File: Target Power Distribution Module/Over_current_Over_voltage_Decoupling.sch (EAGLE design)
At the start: 5 parts

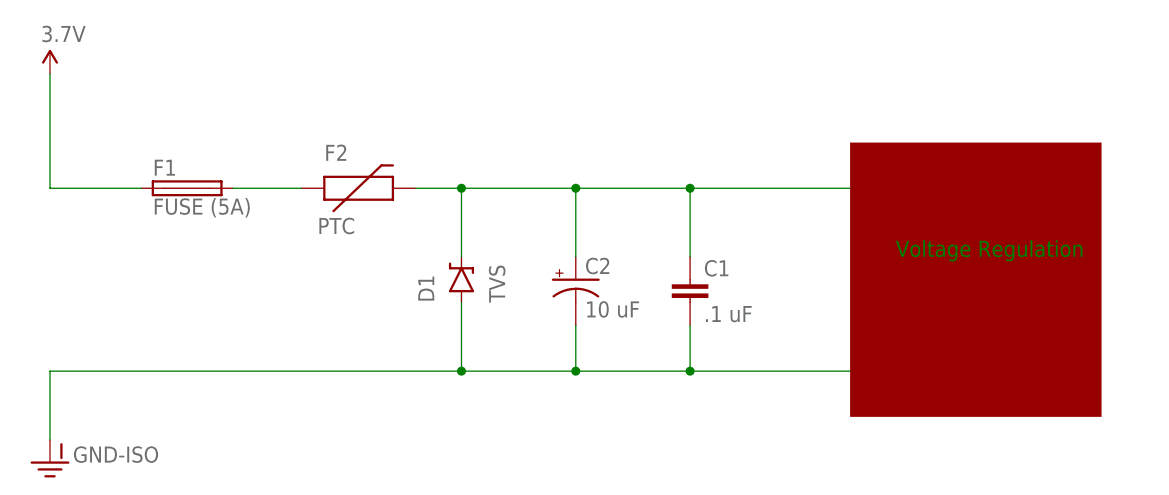
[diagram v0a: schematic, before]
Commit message: Added battery and battery connector
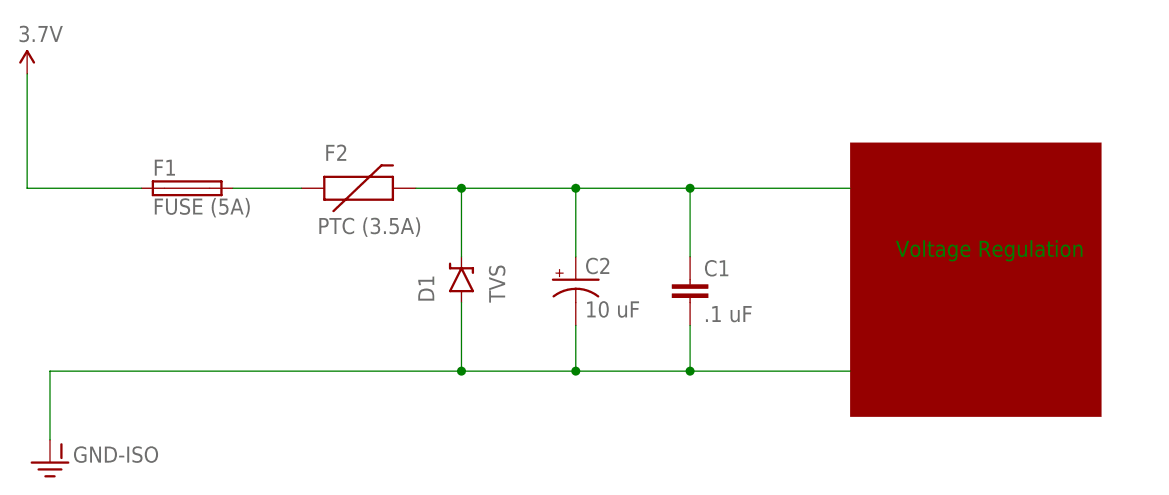
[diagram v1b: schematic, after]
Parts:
- F2: value PTC -> PTC (3.5A)
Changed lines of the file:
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@@
 <grid distance="0.1" unitdist="inch" unit="inch" style="lines" multiple="1" display="no" altdistance="0.01" altunitdist="inch" altunit="inch"/>
 <layers>
-<layer number="1" name="Top" color="4" fill="1" visible="no" active="no"/>
-<layer number="16" name="Bottom" color="1" fill="1" visible="no" active="no"/>
-<layer number="17" name="Pads" color="2" fill="1" visible="no" active="no"/>
-<layer number="18" name="Vias" color="2" fill="1" visible="no" active="no"/>
-<layer number="19" name="Unrouted" color="6" fill="1" visible="no" active="no"/>
-<layer number="20" name="Dimension" color="15" fill="1" visible="no" active="no"/>
-<layer number="21" name="tPlace" color="16" fill="1" visible="no" active="no"/>
-<layer number="22" name="bPlace" color="7" fill="1" visible="no" active="no"/>
-<layer number="23" name="tOrigins" color="15" fill="1" visible="no" active="no"/>
-<layer number="24" name="bOrigins" color="15" fill="1" visible="no" active="no"/>
-<layer number="25" name="tNames" color="7" fill="1" visible="no" active="no"/>
-<layer number="26" name="bNames" color="7" fill="1" visible="no" active="no"/>
-<layer number="27" name="tValues" color="7" fill="1" visible="no" active="no"/>
-<layer number="28" name="bValues" color="7" fill="1" visible="no" active="no"/>
+<layer number="1" name="Top" color="4" fill="1" visible="yes" active="no"/>
+<layer number="16" name="Bottom" color="1" fill="1" visible="yes" active="no"/>
+<layer number="17" name="Pads" color="2" fill="1" visible="yes" active="no"/>
+<layer number="18" name="Vias" color="2" fill="1" visible="yes" active="no"/>
+<layer number="19" name="Unrouted" color="6" fill="1" visible="yes" active="no"/>
+<layer number="20" name="Dimension" color="15" fill="1" visible="yes" active="no"/>
+<layer number="21" name="tPlace" color="16" fill="1" visible="yes" active="no"/>
+<layer number="22" name="bPlace" color="7" fill="1" visible="yes" active="no"/>
+<layer number="23" name="tOrigins" color="15" fill="1" visible="yes" active="no"/>
+<layer number="24" name="bOrigins" color="15" fill="1" visible="yes" active="no"/>
+<layer number="25" name="tNames" color="7" fill="1" visible="yes" active="no"/>
+<layer number="26" name="bNames" color="7" fill="1" visible="yes" active="no"/>
+<layer number="27" name="tValues" color="7" fill="1" visible="yes" active="no"/>
+<layer number="28" name="bValues" color="7" fill="1" visible="yes" active="no"/>
 <layer number="29" name="tStop" color="7" fill="3" visible="no" active="no"/>
 <layer number="30" name="bStop" color="7" fill="6" visible="no" active="no"/>
@@
 <layer number="35" name="tGlue" color="7" fill="4" visible="no" active="no"/>
 <layer number="36" name="bGlue" color="7" fill="5" visible="no" active="no"/>
-<layer number="37" name="tTest" color="7" fill="1" visible="no" active="no"/>
-<layer number="38" name="bTest" color="7" fill="1" visible="no" active="no"/>
+<layer number="37" name="tTest" color="7" fill="1" visible="yes" active="no"/>
+<layer number="38" name="bTest" color="7" fill="1" visible="yes" active="no"/>
 <layer number="39" name="tKeepout" color="4" fill="11" visible="no" active="no"/>
 <layer number="40" name="bKeepout" color="1" fill="11" visible="no" active="no"/>
@@
 <layer number="44" name="Drills" color="7" fill="1" visible="no" active="no"/>
 <layer number="45" name="Holes" color="7" fill="1" visible="no" active="no"/>
-<layer number="46" name="Milling" color="3" fill="1" visible="no" active="no"/>
-<layer number="47" name="Measures" color="7" fill="1" visible="no" active="no"/>
-<layer number="48" name="Document" color="7" fill="1" visible="no" active="no"/>
-<layer number="49" name="Reference" color="7" fill="1" visible="no" active="no"/>
-<layer number="50" name="dxf" color="7" fill="1" visible="no" active="no"/>
-<layer number="51" name="tDocu" color="14" fill="1" visible="no" active="no"/>
-<layer number="52" name="bDocu" color="7" fill="1" visible="no" active="no"/>
-<layer number="53" name="tGND_GNDA" color="7" fill="9" visible="no" active="no"/>
-<layer number="54" name="bGND_GNDA" color="1" fill="9" visible="no" active="no"/>
-<layer number="56" name="wert" color="7" fill="1" visible="no" active="no"/>
-<layer number="57" name="tCAD" color="7" fill="1" visible="no" active="no"/>
-<layer number="59" name="tCarbon" color="7" fill="1" visible="no" active="no"/>
-<layer number="60" name="bCarbon" color="7" fill="1" visible="no" active="no"/>
+<layer number="46" name="Milling" color="3" fill="1" visible="yes" active="no"/>
+<layer number="47" name="Measures" color="7" fill="1" visible="yes" active="no"/>
+<layer number="48" name="Document" color="7" fill="1" visible="yes" active="no"/>
+<layer number="49" name="Reference" color="7" fill="1" visible="yes" active="no"/>
+<layer number="50" name="dxf" color="7" fill="1" visible="yes" active="no"/>
+<layer number="51" name="tDocu" color="14" fill="1" visible="yes" active="no"/>
+<layer number="52" name="bDocu" color="7" fill="1" visible="yes" active="no"/>
+<layer number="53" name="tGND_GNDA" color="7" fill="9" visible="yes" active="no"/>
+<layer number="54" name="bGND_GNDA" color="1" fill="9" visible="yes" active="no"/>
+<layer number="56" name="wert" color="7" fill="1" visible="yes" active="no"/>
+<layer number="57" name="tCAD" color="7" fill="1" visible="yes" active="no"/>
+<layer number="59" name="tCarbon" color="7" fill="1" visible="yes" active="no"/>
+<layer number="60" name="bCarbon" color="7" fill="1" visible="yes" active="no"/>
 <layer number="90" name="Modules" color="5" fill="1" visible="yes" active="yes"/>
 <layer number="91" name="Nets" color="2" fill="1" visible="yes" active="yes"/>
@@
 <part name="D1" library="SparkFun-DiscreteSemi" deviceset="DIODE-ZENER" device="PTH" value="TVS"/>
 <part name="F1" library="fuse" deviceset="FUSE" device="1821" value="FUSE (5A)"/>
-<part name="F2" library="SparkFun-PowerIC" deviceset="PTC" device="PTH" value="PTC"/>
+<part name="F2" library="SparkFun-PowerIC" deviceset="PTC" device="PTH" value="PTC (3.5A)"/>
 <part name="C1" library="SparkFun-Capacitors" deviceset="CAP" device="1206" value=".1 uF"/>
 <part name="C2" library="SparkFun-Passives" deviceset="CAP_POL" device="PTH2" value="10 uF"/>
@@
 <instance part="C2" gate="G$1" x="40.64" y="53.34"/>
 <instance part="GND-ISO1" gate="G$1" x="-17.78" y="33.02"/>
-<instance part="SUPPLY1" gate="G$1" x="-17.78" y="76.2"/>
+<instance part="SUPPLY1" gate="G$1" x="-20.32" y="76.2"/>
 </instances>
 <busses>
@@
 <segment>
 <pinref part="F1" gate="G$1" pin="1"/>
-<wire x1="-7.62" y1="63.5" x2="-17.78" y2="63.5" width="0.1524" layer="91"/>
-<wire x1="-17.78" y1="63.5" x2="-17.78" y2="76.2" width="0.1524" layer="91"/>
+<wire x1="-7.62" y1="63.5" x2="-20.32" y2="63.5" width="0.1524" layer="91"/>
+<wire x1="-20.32" y1="63.5" x2="-20.32" y2="76.2" width="0.1524" layer="91"/>
 <pinref part="SUPPLY1" gate="G$1" pin="VCC"/>
 </segment>

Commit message: Test text
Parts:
- F1: value FUSE (5A) -> FUSE (2A)
- F2: value PTC (3.5A) -> PTC (1.5A)
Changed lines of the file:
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@@
 <grid distance="0.1" unitdist="inch" unit="inch" style="lines" multiple="1" display="no" altdistance="0.01" altunitdist="inch" altunit="inch"/>
 <layers>
-<layer number="1" name="Top" color="4" fill="1" visible="yes" active="no"/>
-<layer number="16" name="Bottom" color="1" fill="1" visible="yes" active="no"/>
-<layer number="17" name="Pads" color="2" fill="1" visible="yes" active="no"/>
-<layer number="18" name="Vias" color="2" fill="1" visible="yes" active="no"/>
-<layer number="19" name="Unrouted" color="6" fill="1" visible="yes" active="no"/>
-<layer number="20" name="Dimension" color="15" fill="1" visible="yes" active="no"/>
-<layer number="21" name="tPlace" color="16" fill="1" visible="yes" active="no"/>
-<layer number="22" name="bPlace" color="7" fill="1" visible="yes" active="no"/>
-<layer number="23" name="tOrigins" color="15" fill="1" visible="yes" active="no"/>
-<layer number="24" name="bOrigins" color="15" fill="1" visible="yes" active="no"/>
-<layer number="25" name="tNames" color="7" fill="1" visible="yes" active="no"/>
-<layer number="26" name="bNames" color="7" fill="1" visible="yes" active="no"/>
-<layer number="27" name="tValues" color="7" fill="1" visible="yes" active="no"/>
-<layer number="28" name="bValues" color="7" fill="1" visible="yes" active="no"/>
+<layer number="1" name="Top" color="4" fill="1" visible="no" active="no"/>
+<layer number="16" name="Bottom" color="1" fill="1" visible="no" active="no"/>
+<layer number="17" name="Pads" color="2" fill="1" visible="no" active="no"/>
+<layer number="18" name="Vias" color="2" fill="1" visible="no" active="no"/>
+<layer number="19" name="Unrouted" color="6" fill="1" visible="no" active="no"/>
+<layer number="20" name="Dimension" color="15" fill="1" visible="no" active="no"/>
+<layer number="21" name="tPlace" color="16" fill="1" visible="no" active="no"/>
+<layer number="22" name="bPlace" color="7" fill="1" visible="no" active="no"/>
+<layer number="23" name="tOrigins" color="15" fill="1" visible="no" active="no"/>
+<layer number="24" name="bOrigins" color="15" fill="1" visible="no" active="no"/>
+<layer number="25" name="tNames" color="7" fill="1" visible="no" active="no"/>
+<layer number="26" name="bNames" color="7" fill="1" visible="no" active="no"/>
+<layer number="27" name="tValues" color="7" fill="1" visible="no" active="no"/>
+<layer number="28" name="bValues" color="7" fill="1" visible="no" active="no"/>
 <layer number="29" name="tStop" color="7" fill="3" visible="no" active="no"/>
 <layer number="30" name="bStop" color="7" fill="6" visible="no" active="no"/>
@@
 <layer number="35" name="tGlue" color="7" fill="4" visible="no" active="no"/>
 <layer number="36" name="bGlue" color="7" fill="5" visible="no" active="no"/>
-<layer number="37" name="tTest" color="7" fill="1" visible="yes" active="no"/>
-<layer number="38" name="bTest" color="7" fill="1" visible="yes" active="no"/>
+<layer number="37" name="tTest" color="7" fill="1" visible="no" active="no"/>
+<layer number="38" name="bTest" color="7" fill="1" visible="no" active="no"/>
 <layer number="39" name="tKeepout" color="4" fill="11" visible="no" active="no"/>
 <layer number="40" name="bKeepout" color="1" fill="11" visible="no" active="no"/>
@@
 <layer number="44" name="Drills" color="7" fill="1" visible="no" active="no"/>
 <layer number="45" name="Holes" color="7" fill="1" visible="no" active="no"/>
-<layer number="46" name="Milling" color="3" fill="1" visible="yes" active="no"/>
-<layer number="47" name="Measures" color="7" fill="1" visible="yes" active="no"/>
-<layer number="48" name="Document" color="7" fill="1" visible="yes" active="no"/>
-<layer number="49" name="Reference" color="7" fill="1" visible="yes" active="no"/>
-<layer number="50" name="dxf" color="7" fill="1" visible="yes" active="no"/>
-<layer number="51" name="tDocu" color="14" fill="1" visible="yes" active="no"/>
-<layer number="52" name="bDocu" color="7" fill="1" visible="yes" active="no"/>
-<layer number="53" name="tGND_GNDA" color="7" fill="9" visible="yes" active="no"/>
-<layer number="54" name="bGND_GNDA" color="1" fill="9" visible="yes" active="no"/>
-<layer number="56" name="wert" color="7" fill="1" visible="yes" active="no"/>
-<layer number="57" name="tCAD" color="7" fill="1" visible="yes" active="no"/>
-<layer number="59" name="tCarbon" color="7" fill="1" visible="yes" active="no"/>
-<layer number="60" name="bCarbon" color="7" fill="1" visible="yes" active="no"/>
+<layer number="46" name="Milling" color="3" fill="1" visible="no" active="no"/>
+<layer number="47" name="Measures" color="7" fill="1" visible="no" active="no"/>
+<layer number="48" name="Document" color="7" fill="1" visible="no" active="no"/>
+<layer number="49" name="Reference" color="7" fill="1" visible="no" active="no"/>
+<layer number="50" name="dxf" color="7" fill="1" visible="no" active="no"/>
+<layer number="51" name="tDocu" color="14" fill="1" visible="no" active="no"/>
+<layer number="52" name="bDocu" color="7" fill="1" visible="no" active="no"/>
+<layer number="53" name="tGND_GNDA" color="7" fill="9" visible="no" active="no"/>
+<layer number="54" name="bGND_GNDA" color="1" fill="9" visible="no" active="no"/>
+<layer number="56" name="wert" color="7" fill="1" visible="no" active="no"/>
+<layer number="57" name="tCAD" color="7" fill="1" visible="no" active="no"/>
+<layer number="59" name="tCarbon" color="7" fill="1" visible="no" active="no"/>
+<layer number="60" name="bCarbon" color="7" fill="1" visible="no" active="no"/>
 <layer number="90" name="Modules" color="5" fill="1" visible="yes" active="yes"/>
 <layer number="91" name="Nets" color="2" fill="1" visible="yes" active="yes"/>
@@
 <parts>
 <part name="D1" library="SparkFun-DiscreteSemi" deviceset="DIODE-ZENER" device="PTH" value="TVS"/>
-<part name="F1" library="fuse" deviceset="FUSE" device="1821" value="FUSE (5A)"/>
-<part name="F2" library="SparkFun-PowerIC" deviceset="PTC" device="PTH" value="PTC (3.5A)"/>
+<part name="F1" library="fuse" deviceset="FUSE" device="1821" value="FUSE (2A)"/>
+<part name="F2" library="SparkFun-PowerIC" deviceset="PTC" device="PTH" value="PTC (1.5A)"/>
 <part name="C1" library="SparkFun-Capacitors" deviceset="CAP" device="1206" value=".1 uF"/>
 <part name="C2" library="SparkFun-Passives" deviceset="CAP_POL" device="PTH2" value="10 uF"/>
